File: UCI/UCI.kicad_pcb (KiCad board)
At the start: 2 copper layers, 24 x 20 mm, 10 parts, among them J1 Conn_02x14_Counter_Clockwise, U1 ESD224DQA

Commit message: Changed the layout of all the sidepanel PCBs to mitigate the problems that arised from the bad previous design.
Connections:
- J1 pad A4: +5V -> Bat-
- J1 pad B4: +5V -> Bat-
- REF** pad 2: (no net) -> GND
- REF** pad 3: GND -> Bat-
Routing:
- net +5V: track 22.5 -> 13.1 mm
- net GND: track 19.8 -> 27.9 mm

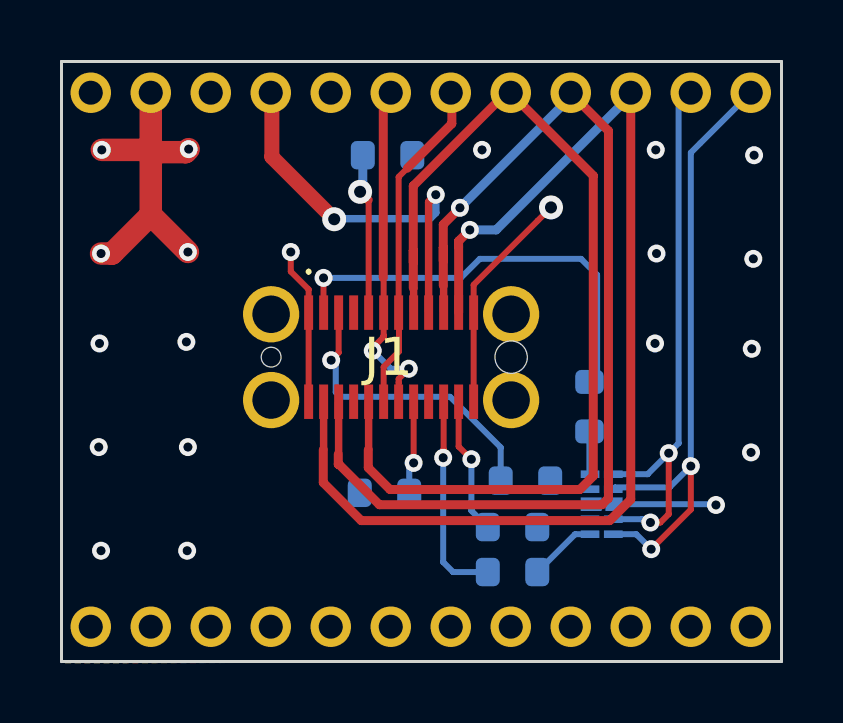
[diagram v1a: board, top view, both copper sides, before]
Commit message: Added a  separate ground for the EDU  sensors and did  some small changes for ordering.
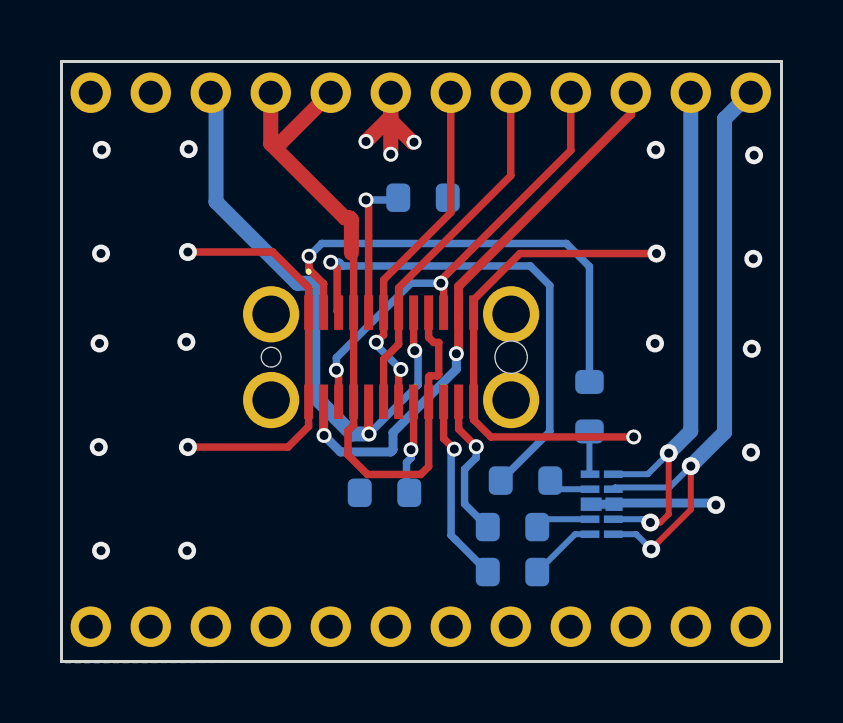
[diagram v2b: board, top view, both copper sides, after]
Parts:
- J1: value Conn_02x14_Counter_Clockwise -> USB_C_Receptacle
- moved R1 1.84 mm to (134.1, 86.1)
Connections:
- net COBC_Debugging_1 renamed UCI_COBC_NOT_RST
- net COBC_Debugging_2 renamed BAT_MIDDLE
- J1 pad A4: Bat- -> +5V
- J1 pad A6: COBC_Flashing_1 -> UCI_COBC_SWDCLK
- J1 pad A7: COBC_Flashing_2 -> UCI_COBC_SWDIO
- J1 pad A8: +3.3V -> Bat-
- J1 pad B4: Bat- -> +5V
- J1 pad B6: COBC_Flashing_1 -> UCI_COBC_SWDCLK
- J1 pad B7: COBC_Flashing_2 -> UCI_COBC_SWDIO
- J1 pad B8: +3.3V -> Bat-
- J1 pad MH1: unconnected-(J1-Pin_13-PadMH1) -> (no net)
- J1 pad MH2: unconnected-(J1-Pin_16-PadMH2) -> (no net)
- J1 pad MH5: unconnected-(J1-Pin_14-PadMH5) -> (no net)
- J1 pad MH6: unconnected-(J1-Pin_15-PadMH6) -> (no net)
- REF** pad 2: GND -> (no net)
- REF** pad 5: GND -> +5V
- REF** pad 6: COBC_Flashing_1 -> GND
- REF** pad 7: COBC_Flashing_2 -> UCI_COBC_SWDCLK
- REF** pad 8: +3.3V -> UCI_COBC_SWDIO
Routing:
- net +3.3V: track 34.1 -> 0.00 mm
- net UCI_COBC_NOT_RST: track 36.0 -> 15.2 mm, vias 1 -> 2
- net Bat-: track 0.00 -> 20.1 mm, vias 0 -> 2
- net BAT_MIDDLE: track 37.5 -> 18.9 mm, vias 1 -> 2
- net UCI_COBC_SWDIO: track 0.00 -> 12.1 mm
- net UCI_COBC_SWDCLK: track 0.00 -> 11.7 mm, vias 0 -> 2
- net +5V: track 13.1 -> 24.8 mm, vias 2 -> 0
- net COBC_Flashing_1: track 11.5 -> 0.00 mm, vias 2 -> 0
- net COBC_Flashing_2: track 11.2 -> 0.00 mm
- net GND: track 27.9 -> 39.1 mm, vias 21 -> 22
- net 2: track 10.2 -> 16.6 mm
- net 1: track 14.4 -> 16.2 mm
- net 3: track 6.99 -> 6.38 mm
- net Net-(J1-CC1): track 5.40 -> 4.90 mm

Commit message: Commit before the order.
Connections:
- J1 pad A11: BAT_MIDDLE -> Bat-
- J1 pad B11: BAT_MIDDLE -> Bat-
- REF** pad 10: BAT_MIDDLE -> UCI_COBC_NOT_RST
- REF** pad 7: UCI_COBC_SWDCLK -> GND
- REF** pad 8: UCI_COBC_SWDIO -> UCI_COBC_SWDCLK
- REF** pad 9: UCI_COBC_NOT_RST -> UCI_COBC_SWDIO
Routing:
- net BAT_MIDDLE: track 18.9 -> 0.00 mm, vias 2 -> 0
- net +5V: track 24.8 -> 43.7 mm
- net Bat-: track 20.1 -> 30.0 mm, vias 2 -> 4
- net UCI_COBC_SWDCLK: track 11.7 -> 15.4 mm
- net UCI_COBC_NOT_RST: track 15.2 -> 16.2 mm
- net UCI_COBC_SWDIO: track 12.1 -> 12.9 mm
- net GND: vias 22 -> 28
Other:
- board text added: "V 2.0"

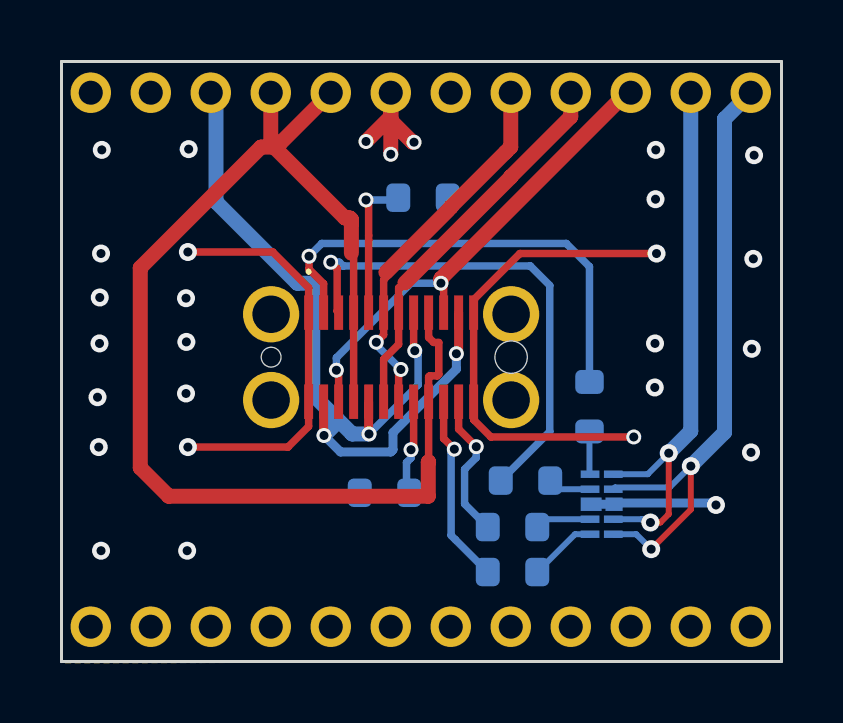
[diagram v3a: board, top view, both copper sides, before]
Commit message: changed all vias from blind to trough and removed the unused pins of the uci connector
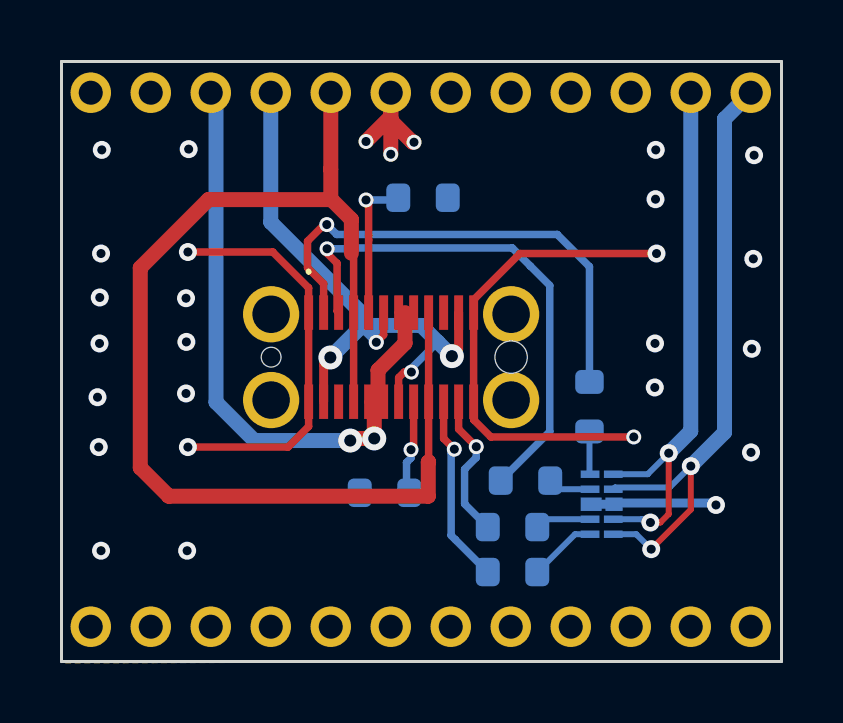
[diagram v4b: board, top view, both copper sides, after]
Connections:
- J1 pad A10: UCI_COBC_NOT_RST -> unconnected-(J1-RX2--PadA10)
- J1 pad A11: Bat- -> Bat+
- J1 pad A6: UCI_COBC_SWDCLK -> Bat+
- J1 pad A7: UCI_COBC_SWDIO -> Bat-
- J1 pad B10: UCI_COBC_NOT_RST -> unconnected-(J1-RX1--PadB10)
- J1 pad B11: Bat- -> Bat+
- J1 pad B6: UCI_COBC_SWDCLK -> Bat+
- J1 pad B7: UCI_COBC_SWDIO -> Bat-
- REF** pad 4: +5V -> Bat+
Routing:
- net Bat+: track 0.00 -> 21.6 mm, vias 0 -> 4
- net UCI_COBC_NOT_RST: track 16.2 -> 0.13 mm, vias 2 -> 0
- net UCI_COBC_SWDCLK: track 15.4 -> 0.00 mm, vias 2 -> 0
- net UCI_COBC_SWDIO: track 12.9 -> 0.00 mm
- net Bat-: track 30.0 -> 22.7 mm, vias 4 -> 2
- net +5V: track 43.7 -> 40.7 mm
- net 1: track 16.2 -> 17.0 mm
- net 2: track 16.6 -> 17.4 mm
